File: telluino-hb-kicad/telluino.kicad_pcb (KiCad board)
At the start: 2 copper layers, 143 x 34 mm, 79 parts, among them J1 6P2C, J2 USB_A, Q1 MMBT3904, U1 LE9641PQC, U2 TISP61089BDR-S, U3 CH340C, U4 TXS0108EPWRG4

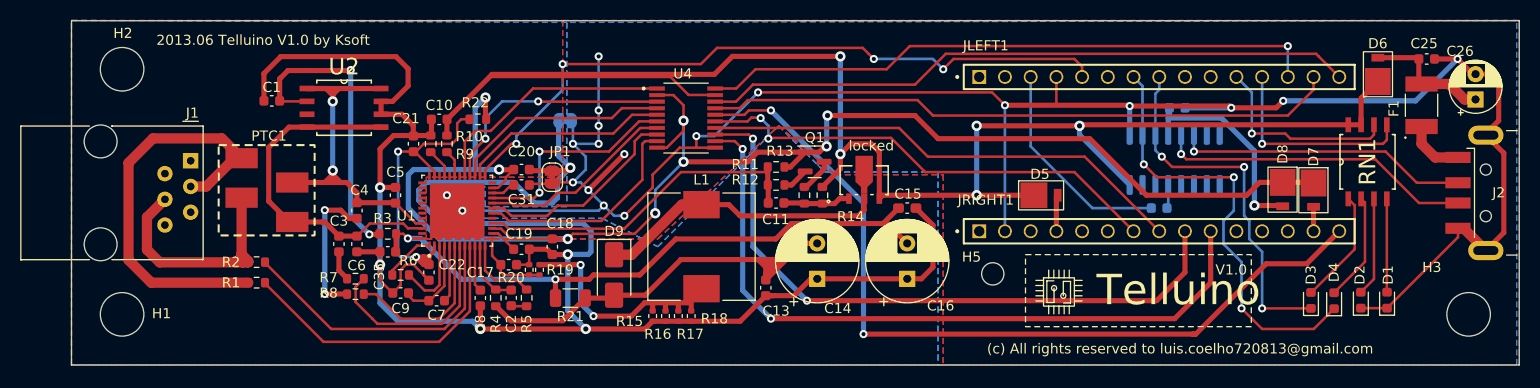
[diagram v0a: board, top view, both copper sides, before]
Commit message: revision after bom review and schematic review
U1 Pin 24 to connect to VCC
Review components to make is more affordable
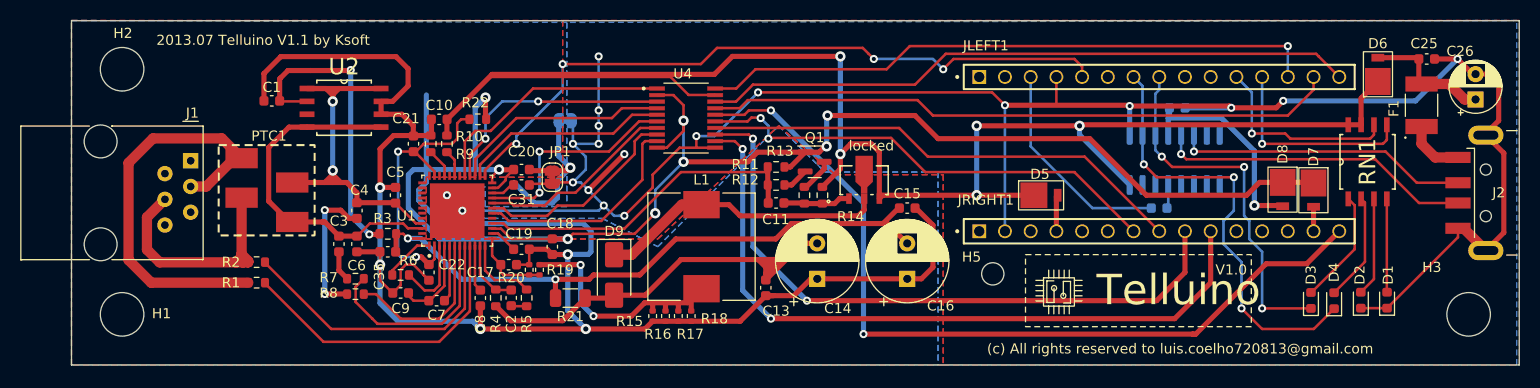
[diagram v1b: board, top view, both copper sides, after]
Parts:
- C1: value 0.1 uF/100V -> 0.1uF/100V
- C11: value 100nF/25V -> 0.1uF/100V
- C15: footprint Capacitor_SMD:C_0603_1608Metric_Pad1.08x0.95mm_HandSolder -> Capacitor_SMD:C_0603_1608Metric
- C18: value 0.1uF/18V -> 0.1uF/100V
- C2, C3, C5, C6: value 22 nF/100V -> 22nF/100V
- C21: value 0.1uF/16V -> 0.1uF/100V
- C22: value 1uF/8.3V -> 1uF/6.3V
- C23, C24: value 0.1uF -> 0.1uF/100V
- C25: value 100nF -> 0.1uF/100V
- C26: value 10uF_16V -> 10uF/25V
- C31, C35: value 0.1 uF/16V -> 0.1uF/100V
- C7, C8, C9: value 4.7 uF/8.3V -> 4.7uF/8.3V
- L1: value 47uH 1.5A -> 22uH 1.8A
- R11: value 10K -> 10K 1%
- R13: value 75R -> 0R
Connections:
- C18 pad 2: +3.3V -> VDDHPI
- C19 pad 2: +3.3V -> VDDHPI
- C20 pad 2: +3.3V -> VDDHPI
- D7 pad 1: +3.3V -> VDDHPI
- D8 pad 1: +3.3V -> VDDHPI
- Q1 pad 1: +3.3V -> VDDHPI
- R11 pad 1: +3.3V -> VDDHPI
- R22 pad 1: +3.3V -> VDDHPI
- U1 pad 14: +3.3V -> VDDHPI
- U1 pad 15: +3.3V -> VDDHPI
- U1 pad 23: +3.3V -> VDDHPI
- U4 pad 10: +3.3V -> VDDHPI
- U4 pad 2: +3.3V -> VDDHPI
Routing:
- net VDDHPI: track 0.00 -> 159.5 mm, vias 0 -> 8
- net +3.3V: track 157.9 -> 0.00 mm, vias 8 -> 0
- net +3.3VA: track 33.2 -> 28.5 mm
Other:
- board text added: "2013.07 Telluino V1.1 by Ksoft"
- board text removed: "2013.06 Telluino V1.0 by Ksoft"

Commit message: reworn resistor array
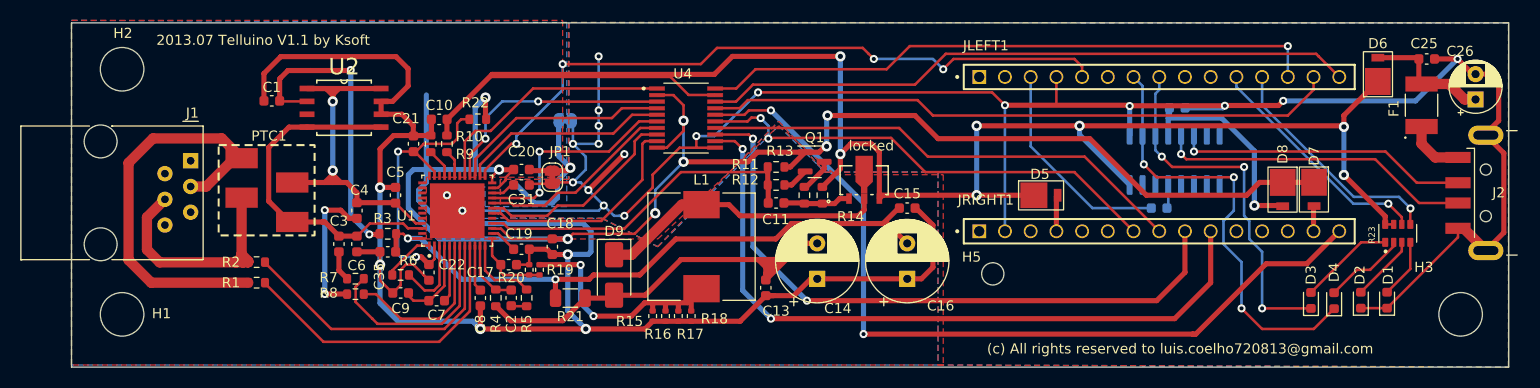
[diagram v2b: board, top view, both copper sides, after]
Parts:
- removed RN1: 4*1K, my_lib:SOIC127P780X210-8N
- removed V1.0: MyLogo, my_lib:MyLogo
- added R23: 4*1K, my_lib:RESCAXE80P320X160X70-8N, F.Cu at (207.0, 105.2)
- moved H3 0.79 mm to (213.2, 113.2)
- moved D7 0.09 mm to (198.7, 100.8)
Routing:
- net +5V: track 167.9 -> 179.5 mm, vias 5 -> 7
- net OP2_LED: track 19.6 -> 23.4 mm
- net Net-(D1-A): track 9.26 -> 5.94 mm
- net Net-(D2-A): track 9.76 -> 6.60 mm
- net OP1_LED: track 20.6 -> 23.3 mm
- net Net-(D4-A): track 10.7 -> 8.17 mm
- net Net-(D3-A): track 11.3 -> 9.43 mm
- net GNDD: track 215.9 -> 215.2 mm
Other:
- board size 143 x 34 mm -> 142 x 34 mm

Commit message: update_for_next_Version
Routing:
- net GNDA: track 200.8 -> 158.5 mm
- net VDDHPI: track 159.5 -> 162.3 mm
- net GNDD: track 215.2 -> 214.9 mm, vias 19 -> 18

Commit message: start_case_design
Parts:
- JLEFT1, JRIGHT1: moved to B.Cu
